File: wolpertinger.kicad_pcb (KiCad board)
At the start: 2 copper layers, 119.6 x 80 mm, 88 parts, among them K1 FRT5, K2 FRT5, Q1 BC549, Q2 BC547, Q3 BC547, SW1 ON/OFF, SW2 DPDT MONO/STEREO, SW3 DPDT HARMONIC/TREMOLO, U1 4093, U10 L78L05_TO92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

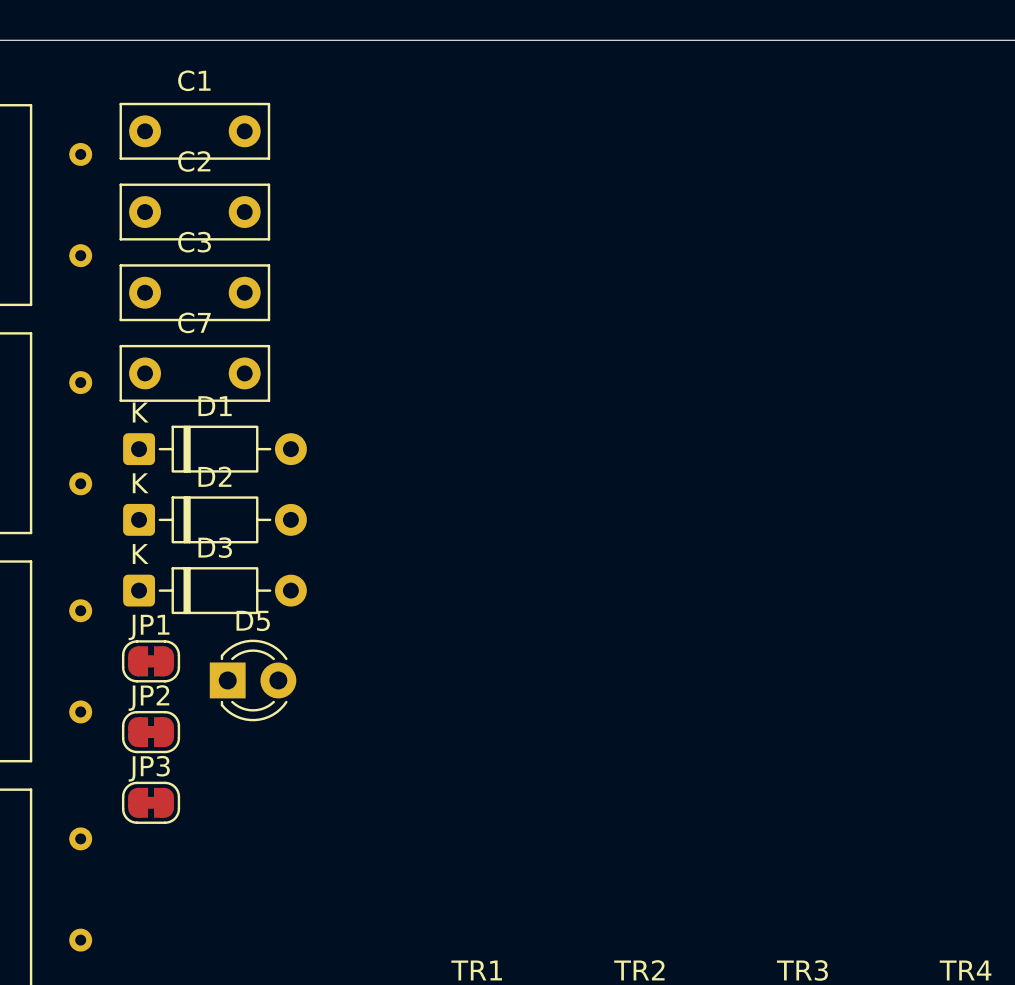
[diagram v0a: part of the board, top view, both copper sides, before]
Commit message: Add capacitors footprint
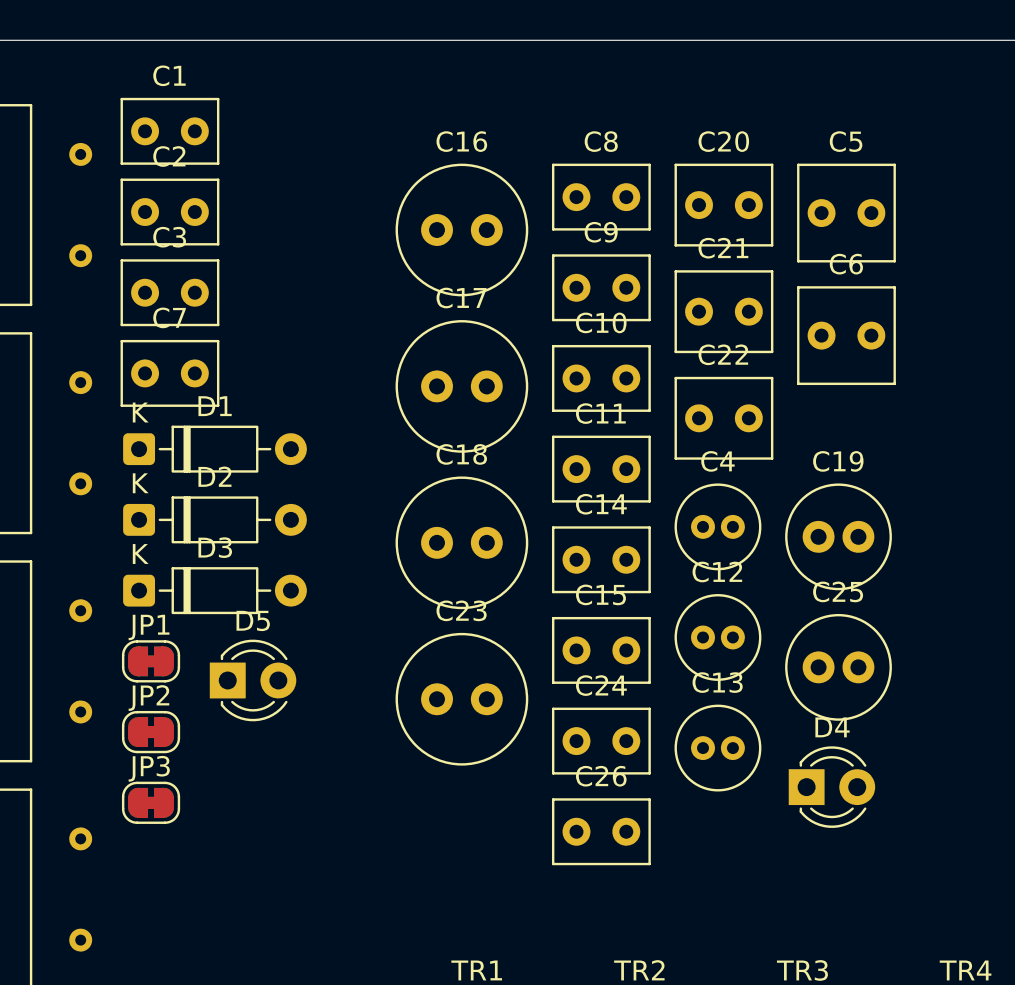
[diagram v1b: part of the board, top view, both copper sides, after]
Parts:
- added C10: 4.7nF, Capacitor_THT:C_Rect_L4.6mm_W3.0mm_P2.50mm_MKS02_FKP02, F.Cu at (163.9, 66.0)
- added C11: 4.7nF, Capacitor_THT:C_Rect_L4.6mm_W3.0mm_P2.50mm_MKS02_FKP02, F.Cu at (163.9, 70.5)
- added C12: 10uF, Capacitor_THT:C_Radial_D4.0mm_H7.0mm_P1.50mm, F.Cu at (170.3, 79.0)
- added C13: 10uF, Capacitor_THT:C_Radial_D4.0mm_H7.0mm_P1.50mm, F.Cu at (170.3, 84.5)
- added C14: 100nF, Capacitor_THT:C_Rect_L4.6mm_W3.0mm_P2.50mm_MKS02_FKP02, F.Cu at (163.9, 75.1)
- added C15: 100nF, Capacitor_THT:C_Rect_L4.6mm_W3.0mm_P2.50mm_MKS02_FKP02, F.Cu at (163.9, 79.6)
- added C16: 100uF, Capacitor_THT:C_Radial_D6.3mm_H11.0mm_P2.50mm, F.Cu at (156.9, 58.5)
- added C17: 100uF, Capacitor_THT:C_Radial_D6.3mm_H11.0mm_P2.50mm, F.Cu at (156.9, 66.4)
- added C18: 47uF, Capacitor_THT:C_Radial_D6.3mm_H11.0mm_P2.50mm, F.Cu at (156.9, 74.2)
- added C19: 47uF, Capacitor_THT:C_Radial_D5.0mm_H11.0mm_P2.00mm, F.Cu at (176.1, 73.9)
- added C20: 330nF, Capacitor_THT:C_Rect_L4.6mm_W3.8mm_P2.50mm_MKS02_FKP02, F.Cu at (170.1, 57.3)
- added C21: 330nF, Capacitor_THT:C_Rect_L4.6mm_W3.8mm_P2.50mm_MKS02_FKP02, F.Cu at (170.1, 62.6)
- added C22: 330nF, Capacitor_THT:C_Rect_L4.6mm_W3.8mm_P2.50mm_MKS02_FKP02, F.Cu at (170.1, 68.0)
- added C23: 100uF, Capacitor_THT:C_Radial_D6.3mm_H11.0mm_P2.50mm, F.Cu at (156.9, 82.1)
- added C24: 100nF, Capacitor_THT:C_Rect_L4.6mm_W3.0mm_P2.50mm_MKS02_FKP02, F.Cu at (163.9, 84.2)
- added C25: 47uF, Capacitor_THT:C_Radial_D5.0mm_H11.0mm_P2.00mm, F.Cu at (176.1, 80.5)
- added C26: 100nF, Capacitor_THT:C_Rect_L4.6mm_W3.0mm_P2.50mm_MKS02_FKP02, F.Cu at (163.9, 88.7)
- added C4: 10uF, Capacitor_THT:C_Radial_D4.0mm_H7.0mm_P1.50mm, F.Cu at (170.3, 73.4)
- added C5: 470nF, Capacitor_THT:C_Rect_L4.6mm_W4.6mm_P2.50mm_MKS02_FKP02, F.Cu at (176.2, 57.7)
- added C6: 470nF, Capacitor_THT:C_Rect_L4.6mm_W4.6mm_P2.50mm_MKS02_FKP02, F.Cu at (176.2, 63.8)
- added C8: 6.8nF, Capacitor_THT:C_Rect_L4.6mm_W3.0mm_P2.50mm_MKS02_FKP02, F.Cu at (163.9, 56.9)
- added C9: 6.8nF, Capacitor_THT:C_Rect_L4.6mm_W3.0mm_P2.50mm_MKS02_FKP02, F.Cu at (163.9, 61.4)
- added D4: STATUS LED, LED_THT:LED_D3.0mm, F.Cu at (175.5, 86.5)
- C1, C2, C3, C7: footprint Capacitor_THT:C_Rect_L7.2mm_W2.5mm_P5.00mm_FKS2_FKP2_MKS2_MKP2 -> Capacitor_THT:C_Rect_L4.6mm_W3.0mm_P2.50mm_MKS02_FKP02

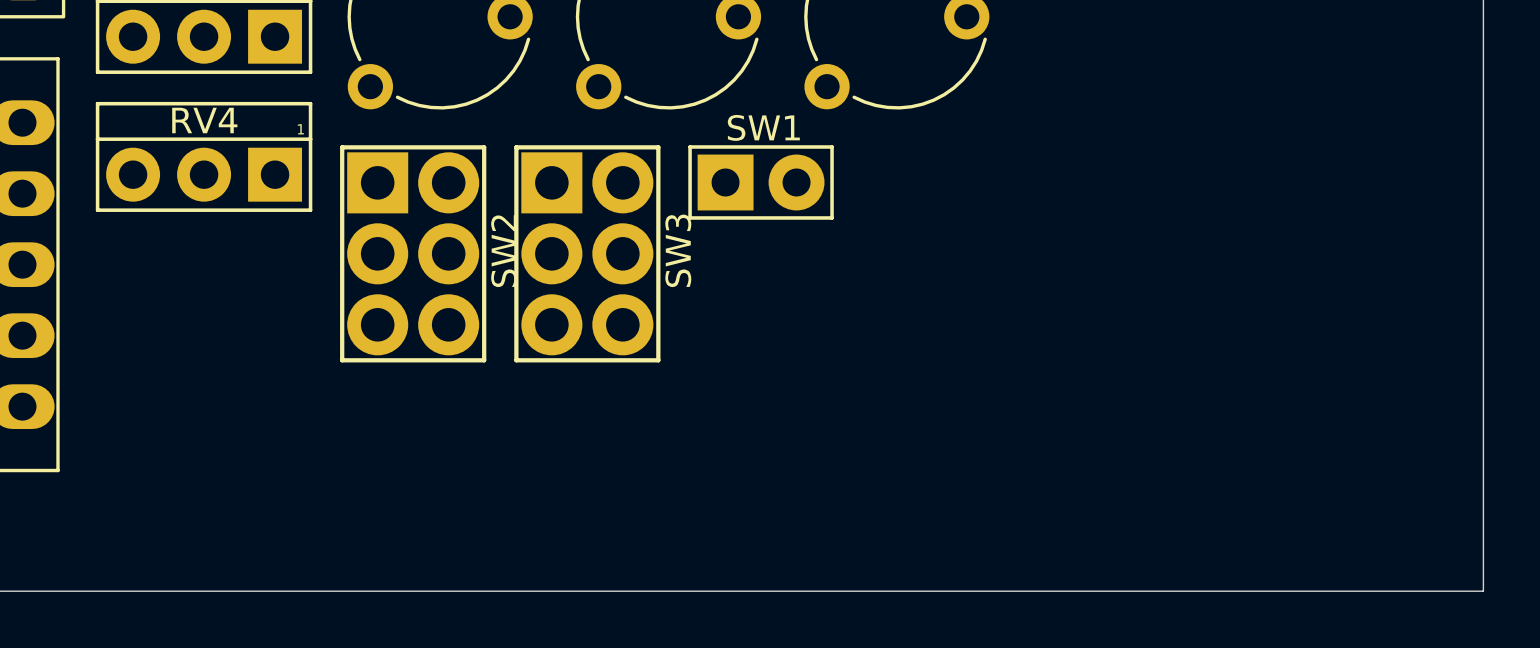
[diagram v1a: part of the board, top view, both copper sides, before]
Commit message: fix footprint pad errors
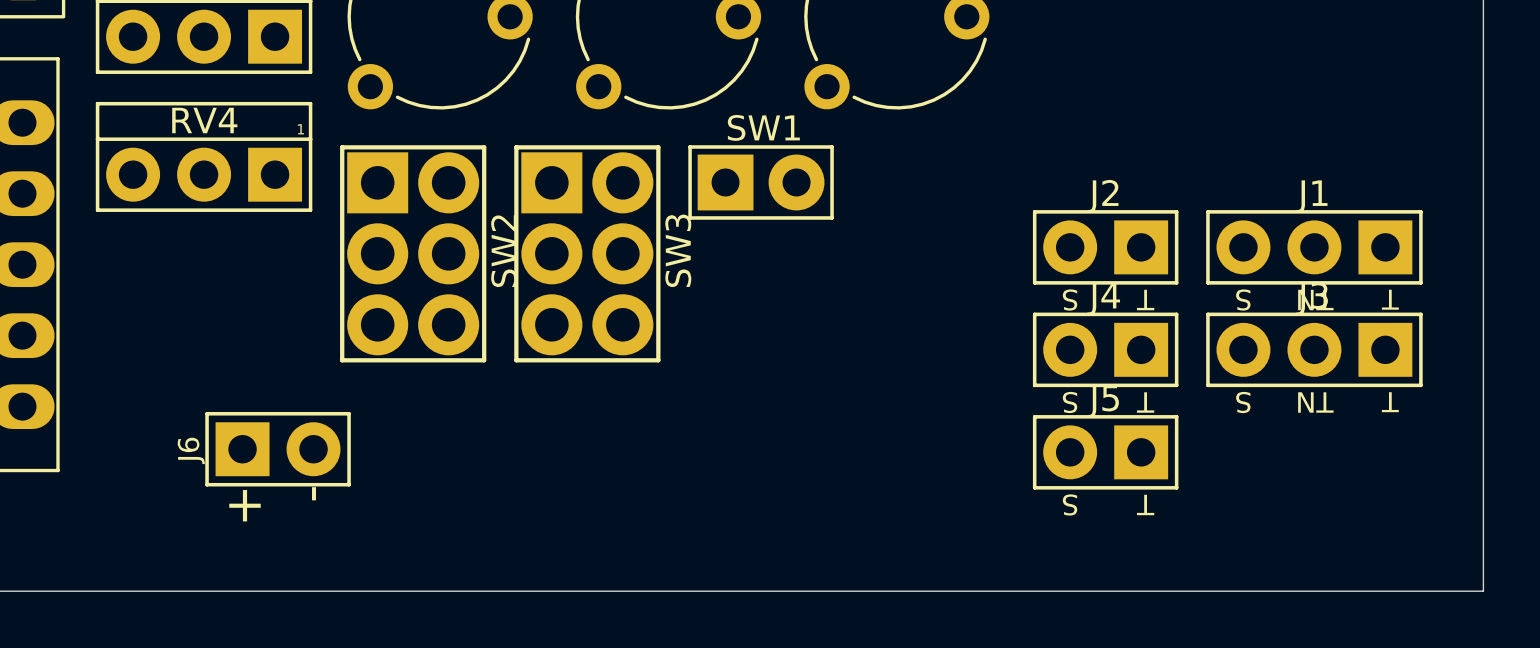
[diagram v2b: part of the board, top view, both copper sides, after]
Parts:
- added J1: RIGHT IN, CustomJacks:Switched Mono Jack, F.Cu at (190.2, 116.7)
- added J2: LEFT IN, jacks:TWO_PADS, F.Cu at (182.8, 116.7)
- added J3: EXT LFO, CustomJacks:Switched Mono Jack, F.Cu at (190.2, 120.4)
- added J4: LEFT OUT, jacks:TWO_PADS, F.Cu at (182.8, 120.4)
- added J5: RIGHT OUT, jacks:TWO_PADS, F.Cu at (182.8, 124.1)
- added J6: Jack-DC, jacks:BATTERY, F.Cu at (153.2, 124.0)

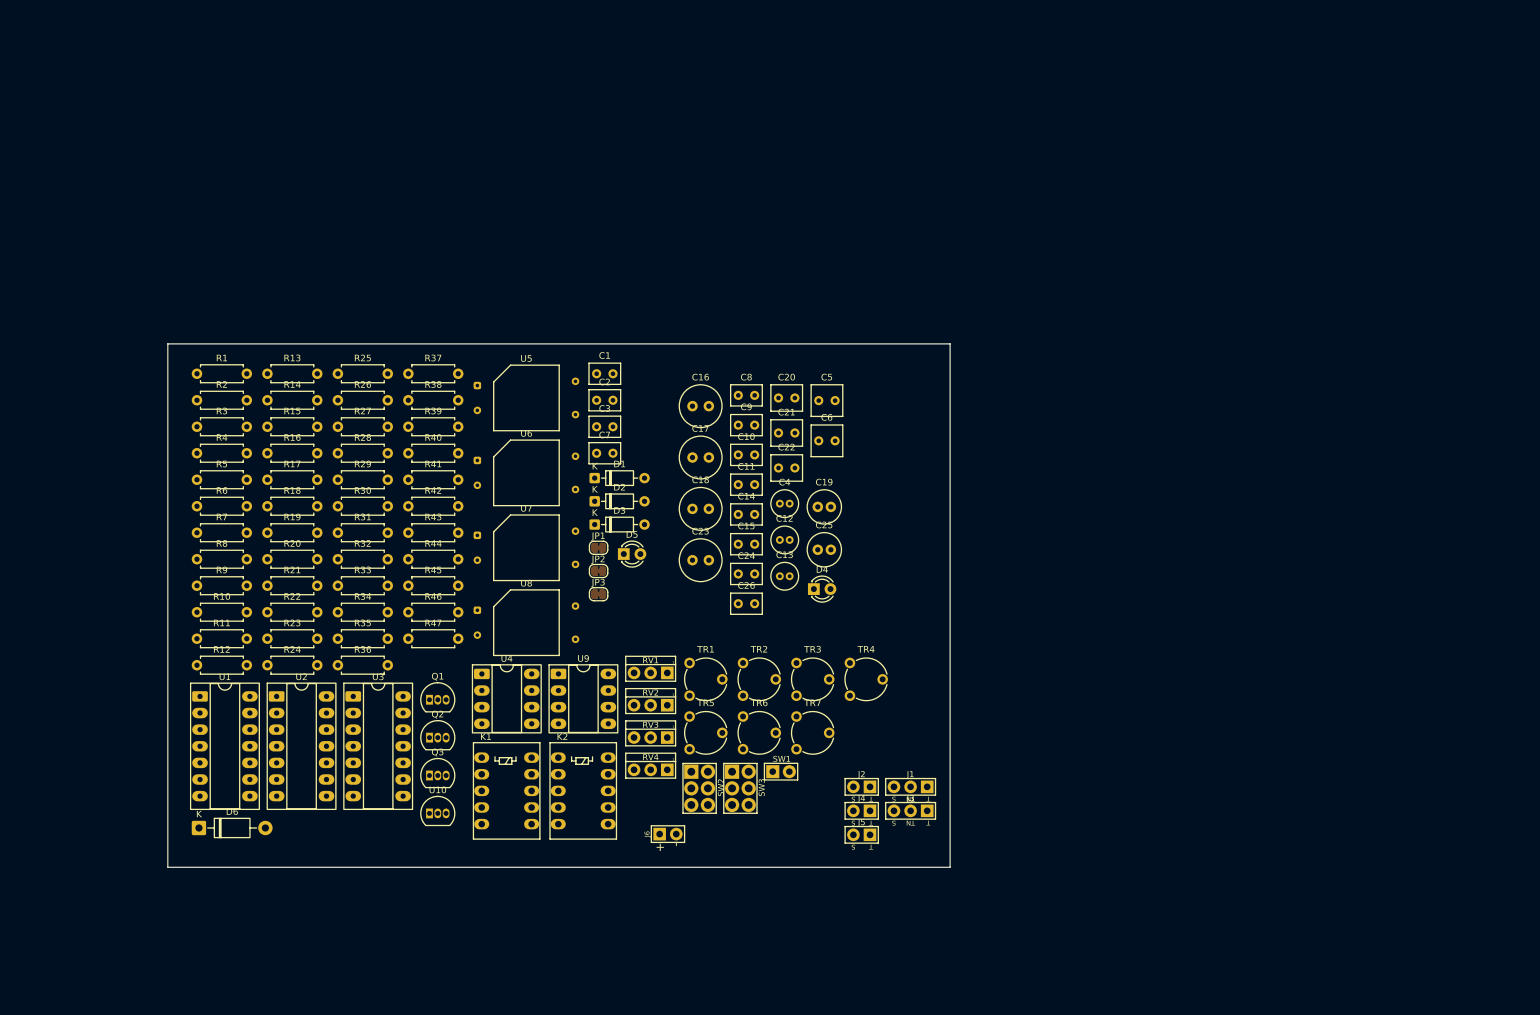
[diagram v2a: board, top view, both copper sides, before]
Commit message: Left channel layout
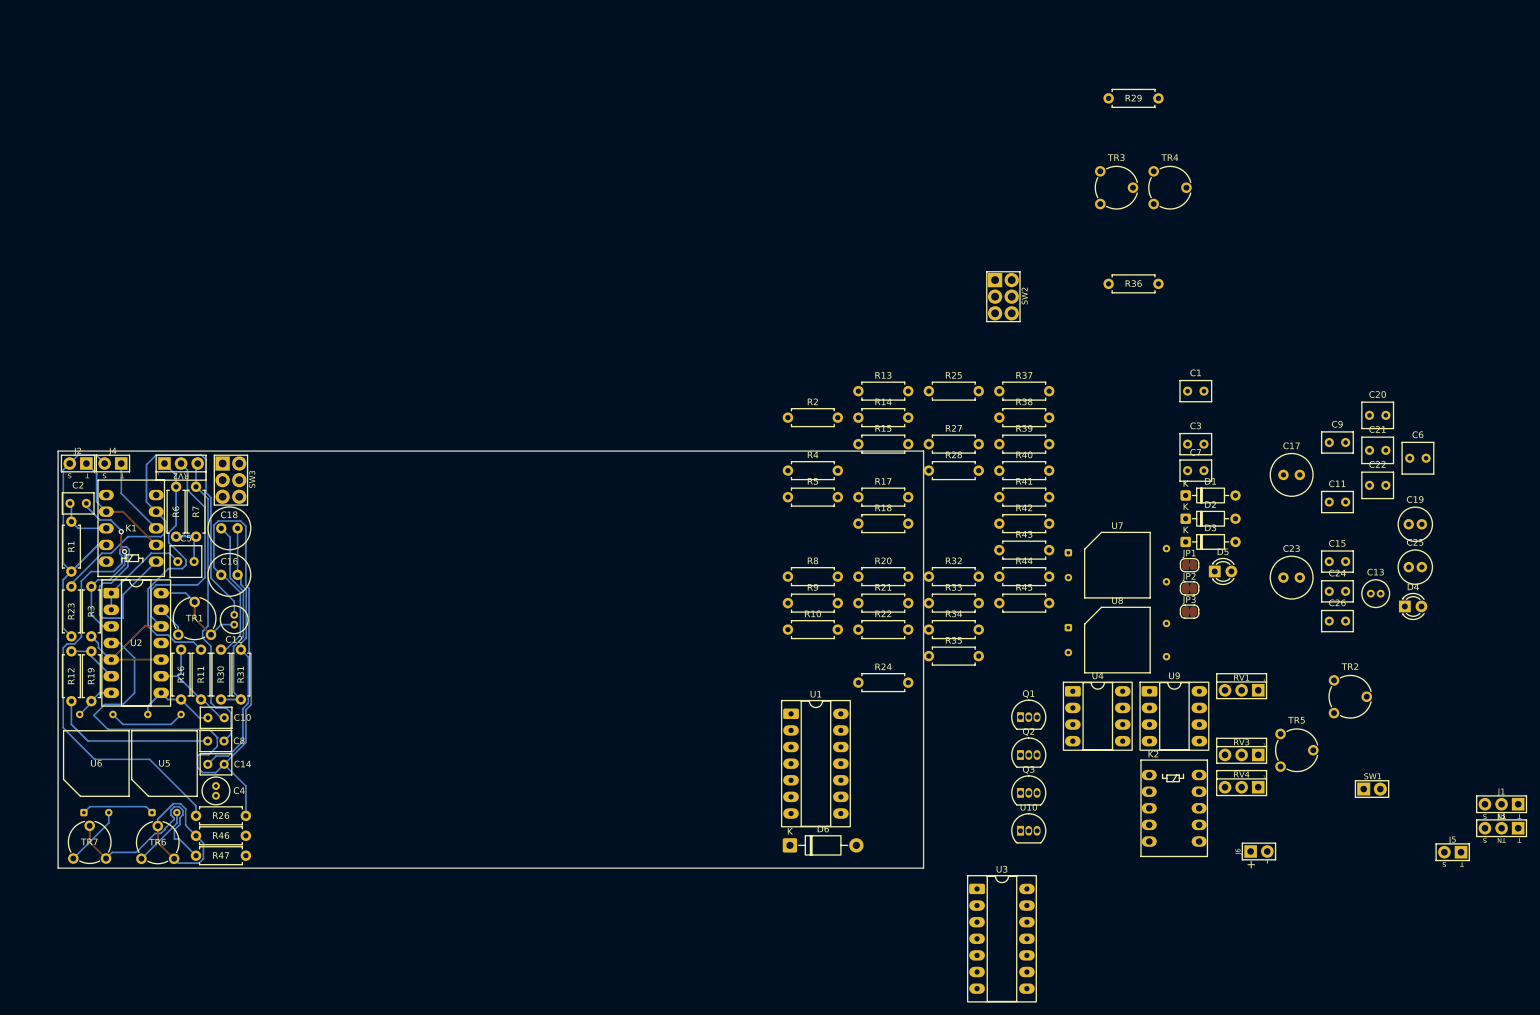
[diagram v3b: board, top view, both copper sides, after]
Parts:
- moved R29 131.4 mm to (220.5, 11.5)
- moved R36 131.4 mm to (220.5, 39.8)
- moved J2 129.6 mm to (63.0, 67.3)
- moved J4 126.2 mm to (68.3, 67.3)
- moved TR7 106.9 mm to (67.3, 127.7), turned to 90 degrees
- moved C5 101.0 mm to (78.2, 82.3)
- moved U3 99.8 mm to (200.4, 132.3)
- moved C4 96.4 mm to (84.1, 116.6), turned to -90 degrees
- moved C8 94.7 mm to (85.3, 109.7), turned to 180 degrees
- moved SW3 91.0 mm to (86.4, 69.8)
- moved D5 90.4 mm to (236.7, 83.8)
- moved SW1 90.4 mm to (260.8, 117.1)
- moved D6 90.4 mm to (171.8, 125.7)
- moved R13 90.4 mm to (182.3, 56.2)
- moved R14 90.4 mm to (182.3, 60.3)
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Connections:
- JP1 pad 2: GND2 -> GND
- JP2 pad 2: GND1 -> GND
- TR3 pad 3: loL -> loR
- TR4 pad 3: hiL -> hiR
- TR6 pad 3: loR -> loL
- TR7 pad 3: hiR -> hiL
- U2 pad 11: GND2 -> GND1
- U2 pad 4: V2 -> V1
- U3 pad 11: GND1 -> GND2
- U3 pad 4: V1 -> V2
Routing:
- net V1: track 0.00 -> 125.2 mm
- net 9V: track 0.00 -> 89.4 mm
- net GND1: track 0.00 -> 82.9 mm
- net Net-(C12-Pad2): track 0.00 -> 66.8 mm
- net Vref1: track 0.00 -> 57.4 mm
- net Net-(C8-Pad1): track 0.00 -> 46.7 mm
- net Net-(R11-Pad1): track 0.00 -> 40.4 mm
- net Net-(R47-Pad2): track 0.00 -> 32.1 mm
- net Vref 1: track 0.00 -> 31.7 mm
- net Net-(U2A-+): track 0.00 -> 27.3 mm, vias 0 -> 2
- net Net-(R46-Pad2): track 0.00 -> 26.4 mm
- net Net-(C8-Pad2): track 0.00 -> 25.4 mm
- net BYPASS L: track 0.00 -> 18.3 mm
- net Net-(U2D--): track 0.00 -> 16.7 mm
- net Net-(U2C--): track 0.00 -> 16.6 mm
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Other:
- board size 119.6 x 80 mm -> 132.3 x 63.8 mm
- board text added: "${REFERENCE}"

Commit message: Right channel
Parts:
- moved J1 193.1 mm to (94.5, 67.5)
- moved J5 181.8 mm to (101.3, 67.5)
- moved TR4 163.8 mm to (98.0, 128.0), turned to 90 degrees
- moved C6 159.1 mm to (108.2, 82.5)
- moved R29 156.4 mm to (111.9, 124.0)
- moved C19 151.4 mm to (115.0, 77.6)
- moved TR3 149.4 mm to (108.5, 128.0), turned to 90 degrees
- moved C9 148.0 mm to (113.8, 110.5)
- moved C11 144.5 mm to (113.8, 107.0)
- moved C15 144.0 mm to (113.8, 114.0)
- moved C13 143.2 mm to (117.5, 92.2), turned to 90 degrees
- moved TR2 141.4 mm to (114.0, 94.0), turned to 90 degrees
- moved C3 140.9 mm to (92.0, 73.5)
- moved RV3 139.6 mm to (108.5, 67.5), turned to 180 degrees
- moved R36 133.4 mm to (119.5, 127.0), turned to 180 degrees
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
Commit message: populate pcb
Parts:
- moved J3 182.1 mm to (107.2, 67.3), turned to 180 degrees
- moved C26 158.0 mm to (96.3, 87.9)
- moved D4 157.4 mm to (113.0, 127.0)
- moved SW1 152.6 mm to (108.5, 127.0)
- moved C20 150.2 mm to (119.1, 111.0), turned to 90 degrees
- moved C21 150.2 mm to (119.1, 116.3), turned to 90 degrees
- moved C22 150.1 mm to (119.1, 121.4), turned to 90 degrees
- moved JP3 142.8 mm to (92.5, 115.6)
- moved D3 138.8 mm to (101.6, 126.0), turned to 180 degrees
- moved C7 138.4 mm to (104.6, 121.2)
- moved C1 136.3 mm to (112.8, 121.2), turned to 180 degrees
- moved TR5 130.6 mm to (120.6, 79.8), turned to 180 degrees
- moved C25 129.9 mm to (136.6, 78.0), turned to 180 degrees
- moved J6 128.7 mm to (129.3, 67.3), turned to 180 degrees
- moved RV1 128.5 mm to (117.1, 67.3)
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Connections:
- C3 pad 2: Net-(U3A-+) -> Net-(U3D-+)
- C6 pad 1: Net-(U3A--) -> Net-(U3D--)
- K2 pad 2: BYPASS R -> GND2
- K2 pad 3: Net-(J5-PadT) -> Net-(C3-Pad1)
- K2 pad 4: Net-(C13-Pad2) -> BYPASS R
- K2 pad 7: BYPASS R -> Net-(C13-Pad2)
- K2 pad 8: Net-(C3-Pad1) -> Net-(J5-PadT)
- K2 pad 9: GND2 -> BYPASS R
- R4 pad 2: Net-(U3A-+) -> Net-(U3D-+)
- TR2 pad 3: Net-(U3D--) -> Net-(U3A--)
- TR3 pad 3: loR -> loL
- TR4 pad 3: hiR -> hiL
- TR6 pad 3: loL -> loR
- TR7 pad 3: hiL -> hiR
- U3 pad 1: Net-(U3A--) -> Net-(C13-Pad1)
- U3 pad 12: Vref2 -> Net-(U3D-+)
- U3 pad 14: Net-(C13-Pad1) -> Net-(U3D--)
- U3 pad 3: Net-(U3A-+) -> Vref2
- U7 pad 4: Net-(U3D--) -> Net-(U3A--)
- U8 pad 4: Net-(U3D--) -> Net-(U3A--)
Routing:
- net V1: track 125.2 -> 0.00 mm
- net 9V: track 89.4 -> 0.00 mm
- net GND1: track 82.9 -> 0.00 mm
- net Net-(C12-Pad2): track 66.8 -> 0.00 mm
- net Vref1: track 57.4 -> 0.00 mm
- net Net-(C8-Pad1): track 46.7 -> 0.00 mm
- net Net-(R11-Pad1): track 40.4 -> 0.00 mm
- net Net-(R47-Pad2): track 32.1 -> 0.00 mm
- net Vref 1: track 31.7 -> 0.00 mm
- net Net-(U2A-+): track 27.3 -> 0.00 mm, vias 2 -> 0
- net Net-(R46-Pad2): track 26.4 -> 0.00 mm
- net Net-(C8-Pad2): track 25.4 -> 0.00 mm
- net BYPASS L: track 18.3 -> 0.00 mm
- net Net-(U2D--): track 16.7 -> 0.00 mm
- net Net-(U2C--): track 16.6 -> 0.00 mm
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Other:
- board size 132.3 x 63.8 mm -> 121.3 x 130.8 mm
